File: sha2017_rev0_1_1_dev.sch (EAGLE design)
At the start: 80 parts, among them IC1 CP210X_USB_UART, IC2 AP7215, IC32 ESP32_AI, Q1 MMBT2222A, Q2 MMBT2222A, Q6 MOSFET-NCHANNELBSS123LT1G, SW801 MCMT5-F-V, X701 2908-05WB-MG

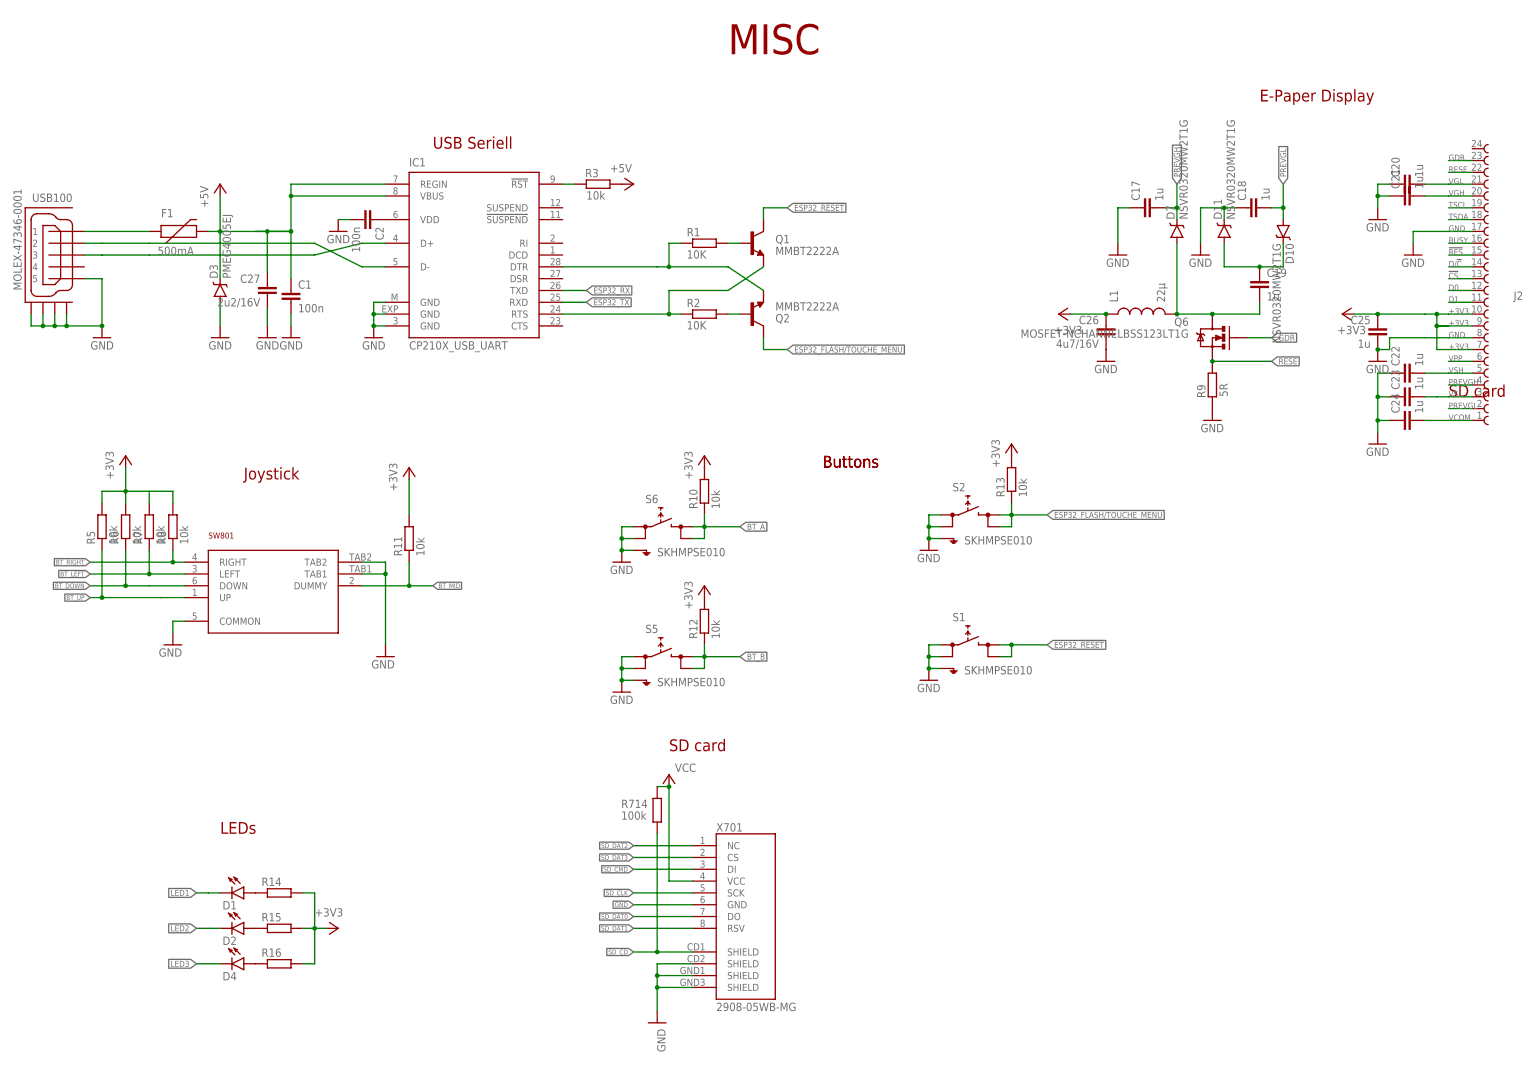
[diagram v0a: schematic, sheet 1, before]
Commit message: add pinout for the lcd added usb status leds
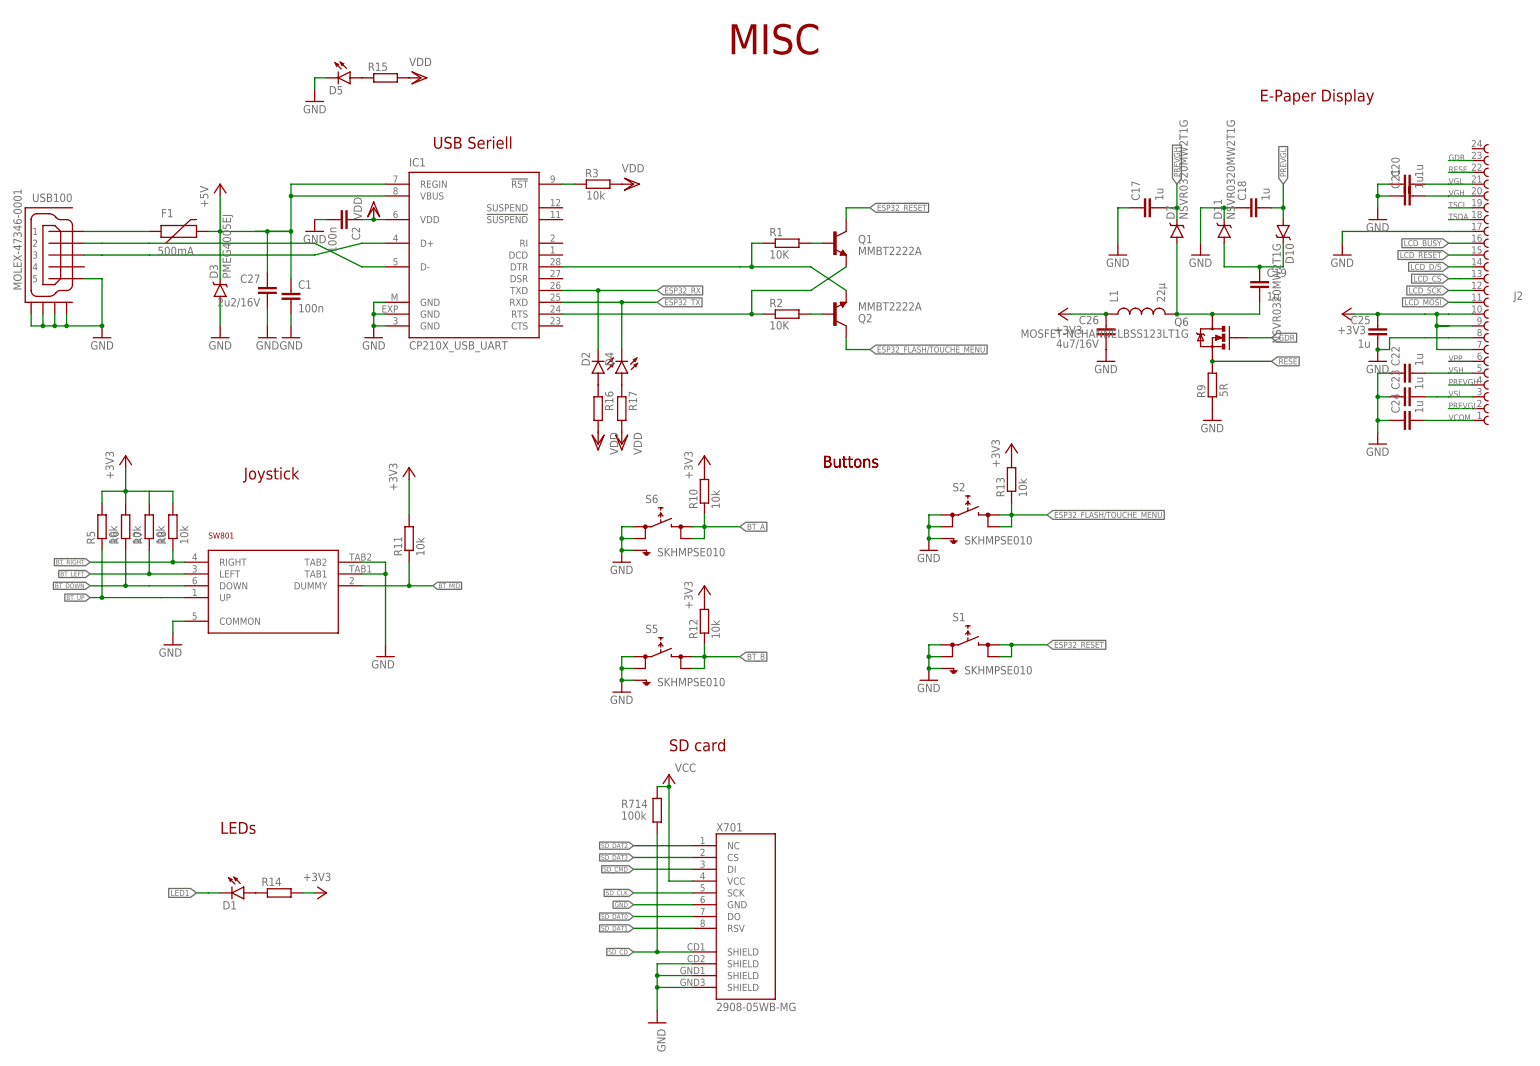
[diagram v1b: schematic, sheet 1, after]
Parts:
- added D5: (no value), SparkFun-LED:LED0603
- added R17: (no value), rcl:R-EU_R0603
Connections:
- removed net !CS: J2.13
- removed net !RES: J2.15
- removed net BUSY: J2.16
- removed net D/!C: J2.14
- removed net D0: J2.12
- removed net D1: J2.11
- removed net LCD_MISO: SJ8.2
- removed net LED2: D2.C, SJ12.2
- removed net LED3: D4.C, SJ14.2
- removed net N$5: C2.1, IC1.VDD
- new net LCD_!RESET: J2.15, SJ12.2
- new net LCD_BUSY: J2.16, SJ14.2
- new net LCD_D/!S: J2.14, SJ8.2
- new net N$28: D4.A, R17.1
- new net VDD: C2.1, IC1.VDD, R15.2, R16.2, R17.2, R3.1
- net +3V3: no longer R15.2, R16.2
- net +5V: no longer R3.1
- net ESP32_RX: now also D2.C
- net ESP32_TX: now also D4.C
- net GND: now also D5.C
- net LCD_CS: now also J2.13
- net LCD_MOSI: now also J2.11
- net LCD_SCK: now also J2.12
- net N$26: now also D5.A; no longer D2.A
- net N$27: now also D2.A; no longer D4.A
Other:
- moved on the sheet: C2, D2, D4, Q1, Q2, R1, R15, R16, R2
